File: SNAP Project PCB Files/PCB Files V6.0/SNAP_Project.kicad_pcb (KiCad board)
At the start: 4 copper layers, 66.7 x 47.2 mm, 107 parts, among them IC1 ADP121-AUJZ30R7, IC2 STM32WB35CCU7A, J1 USB_C_Receptacle_USB2.0, J3 Serial Wire Debug, J4 OLED Screen Conn, Q1 2N7000, Q2 2N7000, Q3 2N7000, Q4 SFH 310, Q5 2N7002KDW_R1_00001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

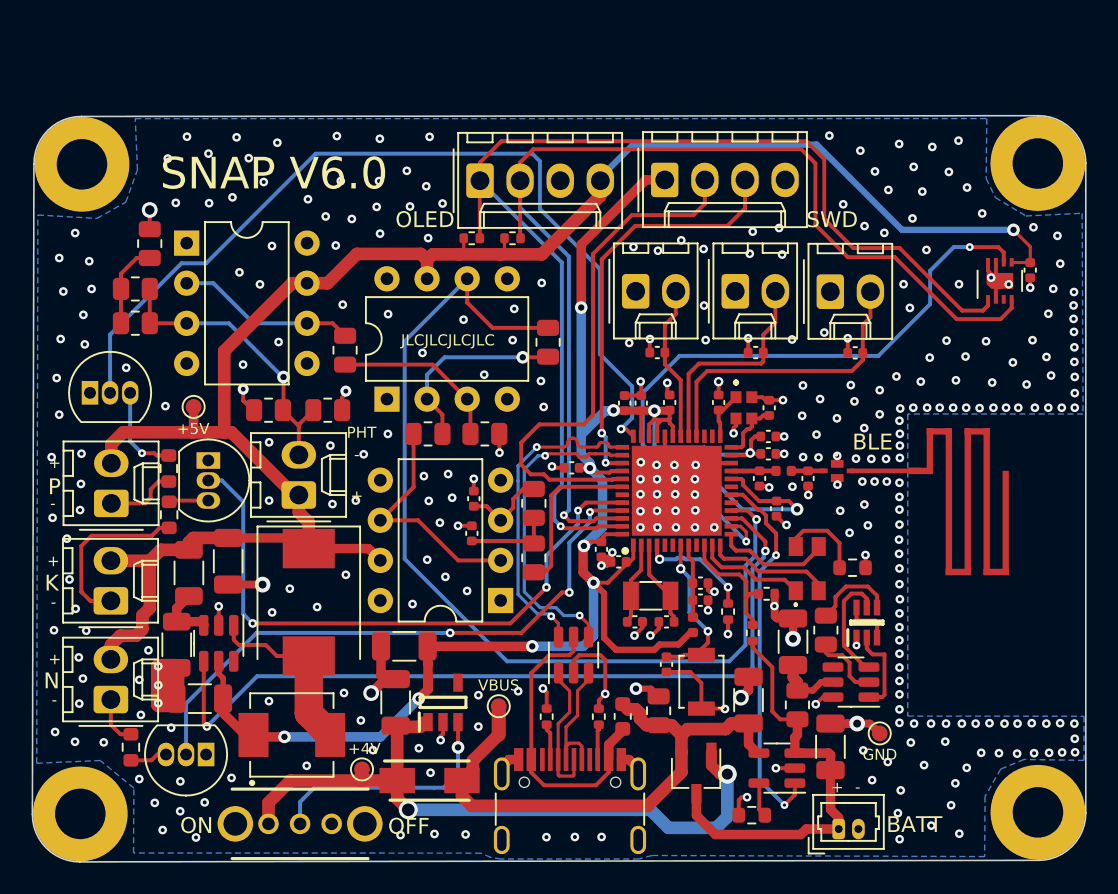
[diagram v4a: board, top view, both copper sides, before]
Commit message: OLED Screen Fix & Board corrections
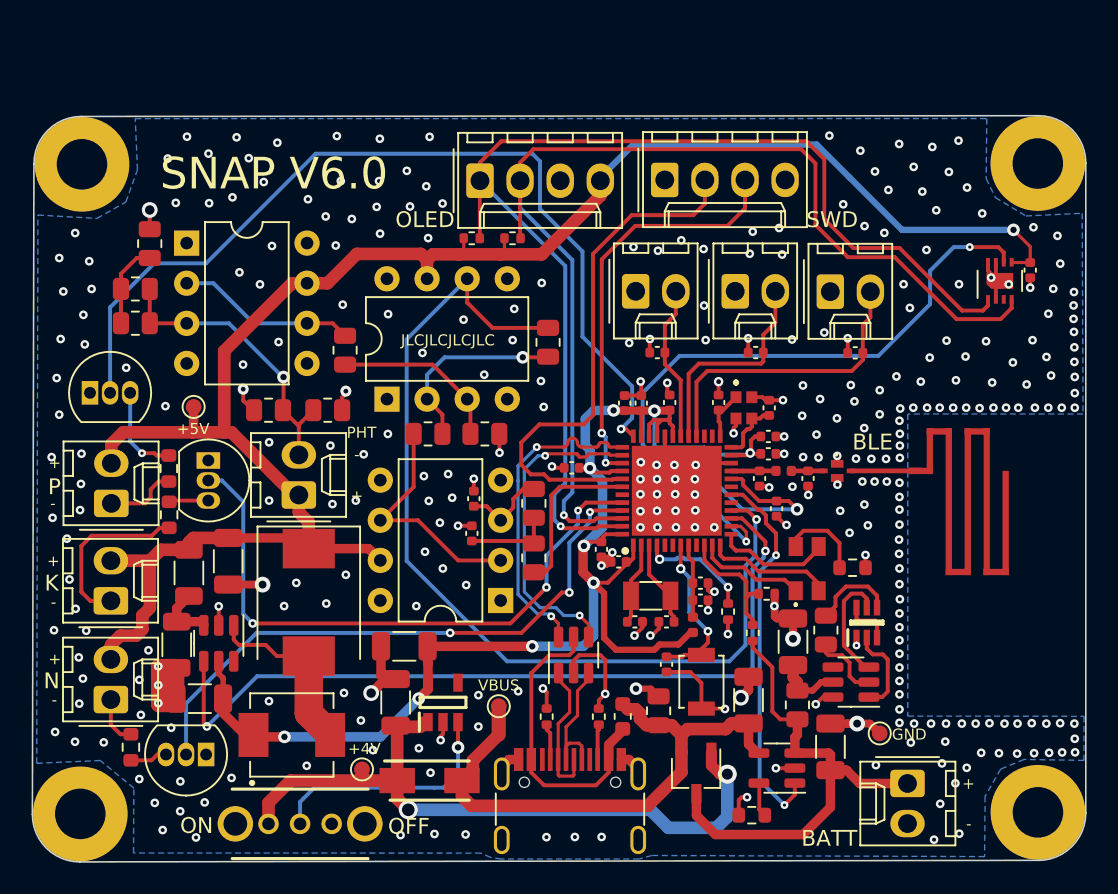
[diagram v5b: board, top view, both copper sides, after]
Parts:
- BT1: footprint Connector_Molex:Molex_PicoBlade_53047-0210_1x02_P1.25mm_Vertical -> Connector_Molex:Molex_KK-254_AE-6410-02A_1x02_P2.54mm_Vertical
- moved G*** 5.89 mm to (115.8, 111.6)
- moved BT1 5.23 mm to (122.2, 117.1), turned to -90 degrees
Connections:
- J3 pad 1: +3V0 -> unconnected-(J3-Pad1)
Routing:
- net +3V0: track 122.9 -> 104.2 mm, vias 11 -> 10
- net +BATT: track 27.2 -> 30.9 mm
- net WP7_EN: track 56.5 -> 57.5 mm
- net GND: vias 342 -> 337
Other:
- board text removed: "+3V0"

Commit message: New changes 1.0
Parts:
- removed C19, C20: 6p, Capacitor_SMD:C_0402_1005Metric
- moved R14 20.6 mm to (131.4, 87.2), turned to 90 degrees
- moved D6 18.8 mm to (129.5, 90.6), turned to 180 degrees
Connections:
- C8 pad 1: +5V -> +3V0
- D2 pad 2: +5V -> +3V0
- D3 pad 2: +5V -> +3V0
- D4 pad 2: +5V -> +3V0
- IC2 pad 9: unconnected-(IC2-Pad9) -> Feedback_VREF
- J4 pad 4: +5V -> +3V0
- R15 pad 1: +5V -> +3V0
- R16 pad 1: +5V -> +3V0
- R23 pad 1: Net-(R23-Pad1) -> Feedback_VREF
- U4 pad 5: +5V -> +3V0
- U5 pad 2: Net-(R23-Pad1) -> Feedback_VREF
- U5 pad 6: Net-(R23-Pad1) -> Feedback_VREF
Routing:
- net +3V0: track 104.2 -> 196.0 mm, vias 10 -> 12
- net +5V: track 117.7 -> 46.9 mm, vias 1 -> 0
- net Feedback_VREF: track 0.00 -> 37.4 mm, vias 0 -> 1
- net RGB_GREEN: track 7.31 -> 33.2 mm, vias 0 -> 2
- net RGB_RED: track 6.96 -> 29.8 mm, vias 0 -> 2
- net RGB_BLUE: track 8.05 -> 28.3 mm, vias 0 -> 2
- net Net-(R23-Pad1): track 15.0 -> 0.00 mm
- net Net-(D6-Pad2): track 5.37 -> 2.02 mm
- net BOOT0: track 7.14 -> 9.68 mm
- net GND: track 94.3 -> 92.3 mm, vias 337 -> 301
- net HSE_OUT: track 4.01 -> 2.74 mm
- net NRST: track 10.1 -> 10.7 mm
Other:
- board text added: "SNAP V6.1"
- board text removed: "SNAP V6.0"

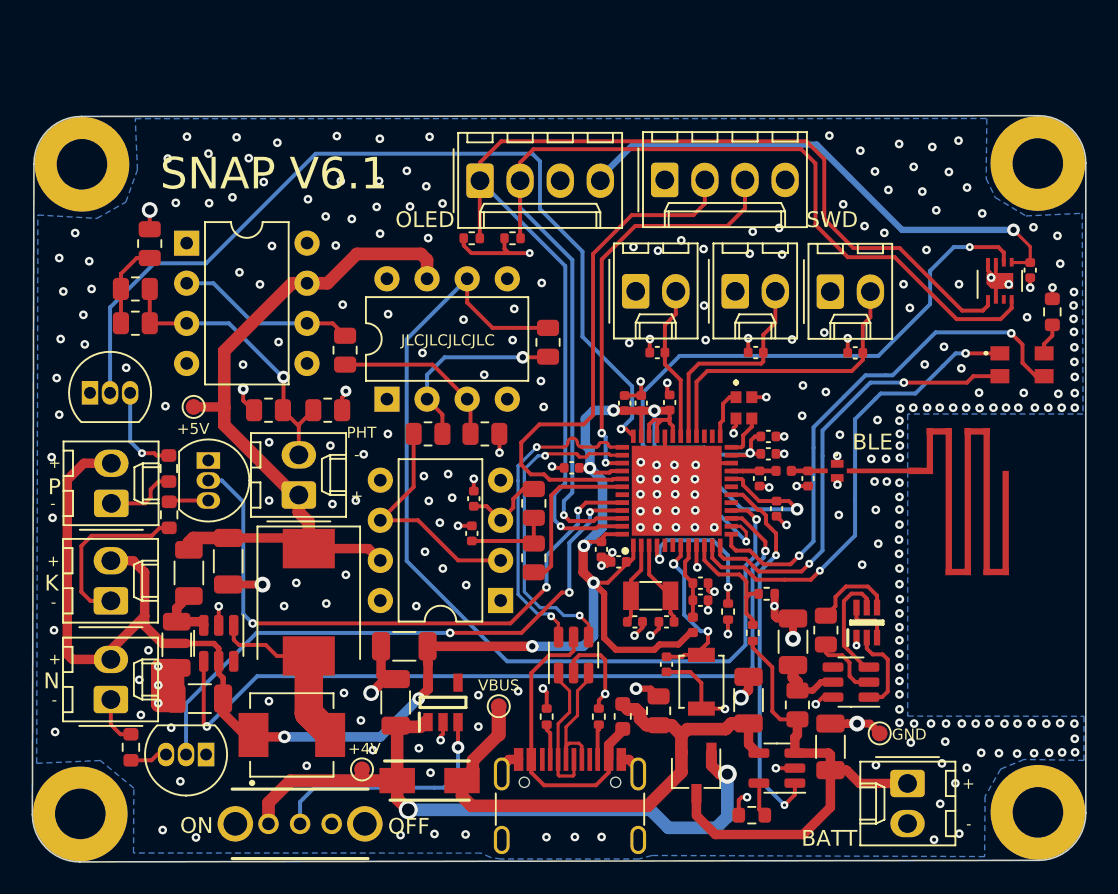
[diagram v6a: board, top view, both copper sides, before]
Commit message: Updated Connectors, LEDs, filter and STM I/O
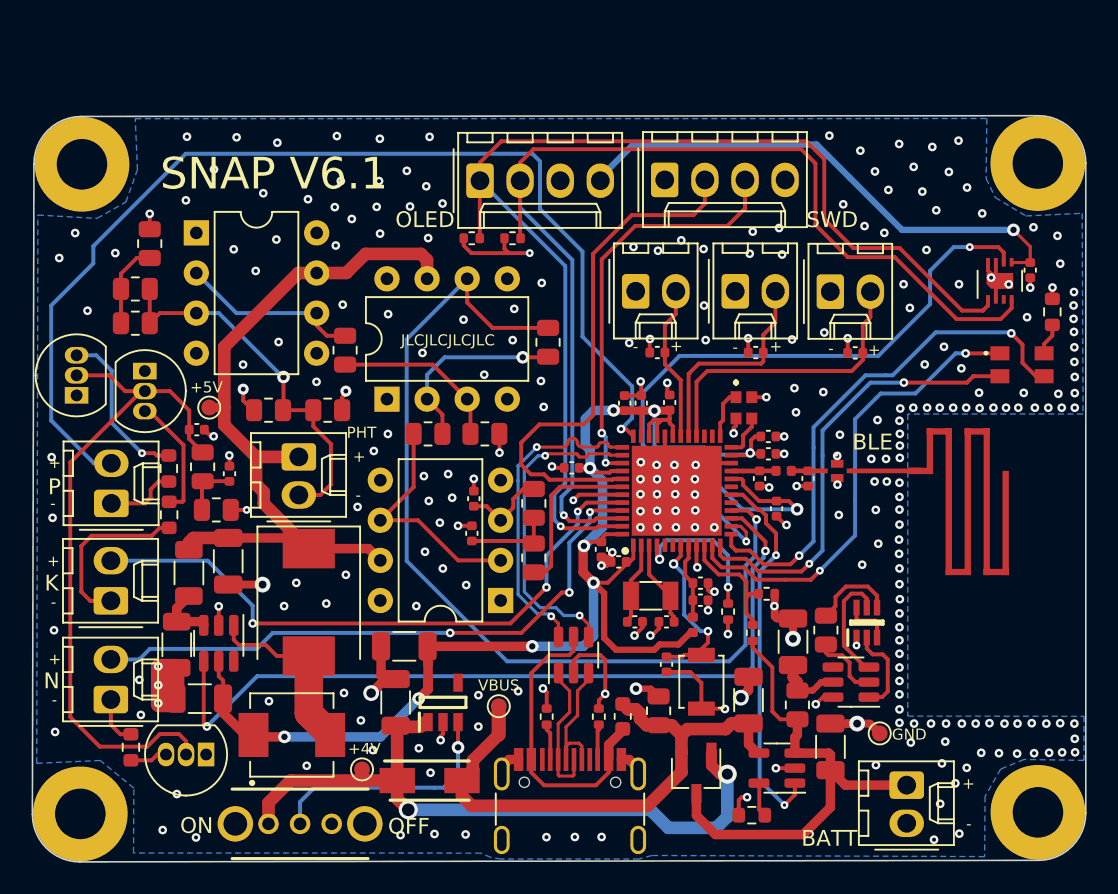
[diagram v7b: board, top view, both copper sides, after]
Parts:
- added C19: 0u1, Capacitor_SMD:C_0402_1005Metric, F.Cu at (79.3, 97.5)
- added C20: 10u, Capacitor_SMD:C_0402_1005Metric, F.Cu at (77.2, 94.7)
- added R29: 1k, Resistor_SMD:R_0805_2012Metric, F.Cu at (78.5, 99.8)
- added R30: 10k, Resistor_SMD:R_0805_2012Metric, F.Cu at (77.6, 97.0)
- R3: value 170 -> 250
- R4: value 120 -> 30
- R5: value 130 -> 40
- moved Q2 6.94 mm to (73.9, 91.0)
- moved BT1 2.52 mm to (122.2, 119.6), turned to 90 degrees
- moved TP2 0.99 mm to (78.0, 93.3)
- moved U6 0.89 mm to (77.2, 82.2)
- moved Q1 0.87 mm to (69.6, 92.5), turned to 90 degrees
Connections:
- D2 pad 2: +3V0 -> WP7_EN
- D3 pad 2: +3V0 -> 4273_EN
- D4 pad 2: +3V0 -> 4261_EN
- IC2 pad 43: unconnected-(IC2-Pad43) -> PWM_LEDS
- Q1 pad 2: WP7_EN -> FILT_PWM
- Q2 pad 2: 4273_EN -> FILT_PWM
- Q3 pad 2: 4261_EN -> FILT_PWM
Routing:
- net FILT_PWM: track 0.00 -> 43.3 mm
- net +3V0: track 196.0 -> 163.3 mm
- net PWM_LEDS: track 0.00 -> 27.6 mm, vias 0 -> 2
- net WP7_EN: track 57.5 -> 68.6 mm
- net Net-(Q4-Pad2): track 18.8 -> 24.1 mm
- net Net-(Q2-Pad3): track 2.51 -> 7.80 mm
- net Net-(Q1-Pad3): track 5.89 -> 10.4 mm
- net Net-(C19-Pad1): track 0.00 -> 3.89 mm
- net +5V: track 46.9 -> 48.6 mm
- net GND: track 92.3 -> 93.6 mm, vias 301 -> 286
- net 4273_EN: track 39.0 -> 39.5 mm

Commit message: Final Commit V 6.1
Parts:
- R23: value 3k3 -> 2k2
- R24: value 1k5 -> 4k7
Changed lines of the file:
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@@
       (drillshape 0)
       (scaleselection 1)
-      (outputdirectory "SNAP Gerbers/")
+      (outputdirectory "SNAP_6.1_Gerbers/")
     )
   )
@@
     (fp_line (start 1 0.625) (end -1 0.625) (layer "F.Fab") (width 0.1))
     (fp_line (start -1 0.625) (end -1 -0.625) (layer "F.Fab") (width 0.1))
-    (pad "1" smd roundrect (at -0.9125 0 180) (size 1.025 1.4) (layers "F.Cu" "F.Paste" "F.Mask") (roundrect_rratio 0.243902)
+    (pad "1" smd roundrect (at -0.9125 0 180) (size 1.025 1.4) (layers "F.Cu" "F.Paste" "F.Mask") (roundrect_rratio 0.243902439)
       (net 53 "Net-(Q4-Pad2)") (pintype "passive"))
-    (pad "2" smd roundrect (at 0.9125 0 180) (size 1.025 1.4) (layers "F.Cu" "F.Paste" "F.Mask") (roundrect_rratio 0.243902)
+    (pad "2" smd roundrect (at 0.9125 0 180) (size 1.025 1.4) (layers "F.Cu" "F.Paste" "F.Mask") (roundrect_rratio 0.243902439)
       (net 89 "Net-(R18-Pad2)") (pintype "passive"))
     (model "${KICAD6_3DMODEL_DIR}/Resistor_SMD.3dshapes/R_0805_2012Metric.wrl"
@@
     (fp_line (start 1 -0.625) (end 1 0.625) (layer "F.Fab") (width 0.1))
     (fp_line (start 1 0.625) (end -1 0.625) (layer "F.Fab") (width 0.1))
-    (pad "1" smd roundrect (at -0.9125 0 180) (size 1.025 1.4) (layers "F.Cu" "F.Paste" "F.Mask") (roundrect_rratio 0.243902)
+    (pad "1" smd roundrect (at -0.9125 0 180) (size 1.025 1.4) (layers "F.Cu" "F.Paste" "F.Mask") (roundrect_rratio 0.243902439)
       (net 53 "Net-(Q4-Pad2)") (pintype "passive"))
-    (pad "2" smd roundrect (at 0.9125 0 180) (size 1.025 1.4) (layers "F.Cu" "F.Paste" "F.Mask") (roundrect_rratio 0.243902)
+    (pad "2" smd roundrect (at 0.9125 0 180) (size 1.025 1.4) (layers "F.Cu" "F.Paste" "F.Mask") (roundrect_rratio 0.243902439)
       (net 89 "Net-(R18-Pad2)") (pintype "passive"))
     (model "${KICAD6_3DMODEL_DIR}/Resistor_SMD.3dshapes/R_0805_2012Metric.wrl"
@@
     (fp_line (start -1.27 2.88) (end 3.81 2.88) (layer "F.Fab") (width 0.1))
     (fp_line (start 3.81 -2.92) (end -1.27 -2.92) (layer "F.Fab") (width 0.1))
-    (pad "1" thru_hole roundrect (at 2.413 0 90) (size 1.74 2.19) (drill 1.19) (layers *.Cu *.Mask) (roundrect_rratio 0.143678)
+    (pad "1" thru_hole roundrect (at 2.413 0 90) (size 1.74 2.19) (drill 1.19) (layers *.Cu *.Mask) (roundrect_rratio 0.1436781609)
       (net 48 "+BATT") (pinfunction "+") (pintype "passive"))
     (pad "2" thru_hole oval (at 0 0 90) (size 1.74 2.19) (drill 1.19) (layers *.Cu *.Mask)
@@
     (fp_line (start -1 -0.625) (end 1 -0.625) (layer "F.Fab") (width 0.1))
     (fp_line (start 1 0.625) (end -1 0.625) (layer "F.Fab") (width 0.1))
-    (pad "1" smd roundrect (at -0.9125 0 90) (size 1.025 1.4) (layers "F.Cu" "F.Paste" "F.Mask") (roundrect_rratio 0.243902)
+    (pad "1" smd roundrect (at -0.9125 0 90) (size 1.025 1.4) (layers "F.Cu" "F.Paste" "F.Mask") (roundrect_rratio 0.243902439)
       (net 89 "Net-(R18-Pad2)") (pintype "passive"))
-    (pad "2" smd roundrect (at 0.9125 0 90) (size 1.025 1.4) (layers "F.Cu" "F.Paste" "F.Mask") (roundrect_rratio 0.243902)
+    (pad "2" smd roundrect (at 0.9125 0 90) (size 1.025 1.4) (layers "F.Cu" "F.Paste" "F.Mask") (roundrect_rratio 0.243902439)
       (net 2 "GND") (pintype "passive"))
     (model "${KICAD6_3DMODEL_DIR}/Resistor_SMD.3dshapes/R_0805_2012Metric.wrl"
@@
     (fp_line (start -1 0.625) (end -1 -0.625) (layer "F.Fab") (width 0.1))
     (fp_line (start -1 -0.625) (end 1 -0.625) (layer "F.Fab") (width 0.1))
-    (pad "1" smd roundrect locked (at -0.9125 0 90) (size 1.025 1.4) (layers "F.Cu" "F.Paste" "F.Mask") (roundrect_rratio 0.243902)
+    (pad "1" smd roundrect locked (at -0.9125 0 90) (size 1.025 1.4) (layers "F.Cu" "F.Paste" "F.Mask") (roundrect_rratio 0.243902439)
       (net 18 "Net-(C19-Pad1)") (pintype "passive"))
-    (pad "2" smd roundrect locked (at 0.9125 0 90) (size 1.025 1.4) (layers "F.Cu" "F.Paste" "F.Mask") (roundrect_rratio 0.243902)
+    (pad "2" smd roundrect locked (at 0.9125 0 90) (size 1.025 1.4) (layers "F.Cu" "F.Paste" "F.Mask") (roundrect_rratio 0.243902439)
       (net 68 "FILT_PWM") (pintype "passive"))
     (model "${KICAD6_3DMODEL_DIR}/Resistor_SMD.3dshapes/R_0805_2012Metric.wrl"
@@
       (effects (font (size 1 1) (thickness 0.15)))
     )
-    (fp_text value "3k3" (at 0 1.65) (layer "F.Fab") hide
+    (fp_text value "2k2" (at 0 1.65) (layer "F.Fab") hide
       (effects (font (size 1 1) (thickness 0.15)))
     )
@@
       (effects (font (size 1 1) (thickness 0.15)))
     )
-    (fp_text value "1k5" (at 0 1.65 90) (layer "F.Fab") hide
+    (fp_text value "4k7" (at 0 1.65 90) (layer "F.Fab") hide
       (effects (font (size 1 1) (thickness 0.15)))
     )
@@
     (fp_line (start 1 -0.625) (end 1 0.625) (layer "F.Fab") (width 0.1))
     (fp_line (start 1 0.625) (end -1 0.625) (layer "F.Fab") (width 0.1))
-    (pad "1" smd roundrect locked (at -0.9125 0 180) (size 1.025 1.4) (layers "F.Cu" "F.Paste" "F.Mask") (roundrect_rratio 0.243902)
+    (pad "1" smd roundrect locked (at -0.9125 0 180) (size 1.025 1.4) (layers "F.Cu" "F.Paste" "F.Mask") (roundrect_rratio 0.243902439)
       (net 92 "PWM_LEDS") (pintype "passive"))
-    (pad "2" smd roundrect locked (at 0.9125 0 180) (size 1.025 1.4) (layers "F.Cu" "F.Paste" "F.Mask") (roundrect_rratio 0.243902)
+    (pad "2" smd roundrect locked (at 0.9125 0 180) (size 1.025 1.4) (layers "F.Cu" "F.Paste" "F.Mask") (roundrect_rratio 0.243902439)
       (net 18 "Net-(C19-Pad1)") (pintype "passive"))
     (model "${KICAD6_3DMODEL_DIR}/Resistor_SMD.3dshapes/R_0805_2012Metric.wrl"
@@
       (effects (font (size 1 1) (thickness 0.15)))
     )
-    (fp_line (start 2.29 1.46) (end 2.54 1.99) (layer "F.SilkS") (width 0.12))
+    (fp_line (start 1.74 -2.43) (end 3.34 -2.43) (layer "F.SilkS") (width 0.12))
     (fp_line (start -1.67 -2) (end -1.67 2) (layer "F.SilkS") (width 0.12))
-    (fp_line (start -1.38 -3.03) (end -1.38 2.99) (layer "F.SilkS") (width 0.12))
     (fp_line (start -0.8 -3.03) (end -0.8 -2.43) (layer "F.SilkS") (width 0.12))
+    (fp_line (start -1.38 -3.03) (end -1.38 2.99) (layer "F.SilkS") (width 0.12))
+    (fp_line (start 2.29 2.99) (end 2.29 1.99) (layer "F.SilkS") (width 0.12))
+    (fp_line (start 2.29 1.46) (end 2.54 1.99) (layer "F.SilkS") (width 0.12))
     (fp_line (start 3.92 2.99) (end 3.92 -3.03) (layer "F.SilkS") (width 0.12))
-    (fp_line (start 1.74 -2.43) (end 3.34 -2.43) (layer "F.SilkS") (width 0.12))
+    (fp_line (start 3.34 -2.43) (end 3.34 -3.03) (layer "F.SilkS") (width 0.12))
     (fp_line (start 2.54 1.99) (end 2.54 2.99) (layer "F.SilkS") (width 0.12))
     (fp_line (start 0.25 1.46) (end 2.29 1.46) (layer "F.SilkS") (width 0.12))
-    (fp_line (start 1.74 -3.03) (end 1.74 -2.43) (layer "F.SilkS") (width 0.12))
-    (fp_line (start -0.8 -2.43) (end 0.8 -2.43) (layer "F.SilkS") (width 0.12))
-    (fp_line (start 3.34 -2.43) (end 3.34 -3.03) (layer "F.SilkS") (width 0.12))
-    (fp_line (start -1.38 2.99) (end 3.92 2.99) (layer "F.SilkS") (width 0.12))
+    (fp_line (start 0.25 2.99) (end 0.25 1.99) (layer "F.SilkS") (width 0.12))
     (fp_line (start 0.8 -2.43) (end 0.8 -3.03) (layer "F.SilkS") (width 0.12))
+    (fp_line (start -1.38 2.99) (end 3.92 2.99) (layer "F.SilkS") (width 0.12))
     (fp_line (start 0 2.99) (end 0 1.99) (layer "F.SilkS") (width 0.12))
+    (fp_line (start -0.8 -2.43) (end 0.8 -2.43) (layer "F.SilkS") (width 0.12))
     (fp_line (start 0 1.99) (end 2.54 1.99) (layer "F.SilkS") (width 0.12))
     (fp_line (start 0 1.99) (end 0.25 1.46) (layer "F.SilkS") (width 0.12))
-    (fp_line (start 0.25 2.99) (end 0.25 1.99) (layer "F.SilkS") (width 0.12))
-    (fp_line (start 2.29 2.99) (end 2.29 1.99) (layer "F.SilkS") (width 0.12))
+    (fp_line (start 1.74 -3.03) (end 1.74 -2.43) (layer "F.SilkS") (width 0.12))
     (fp_line (start 3.92 -3.03) (end -1.38 -3.03) (layer "F.SilkS") (width 0.12))
+    (fp_line (start -1.77 -3.42) (end -1.77 3.38) (layer "F.CrtYd") (width 0.05))
     (fp_line (start 4.31 3.38) (end 4.31 -3.42) (layer "F.CrtYd") (width 0.05))
     (fp_line (start -1.77 3.38) (end 4.31 3.38) (layer "F.CrtYd") (width 0.05))
-    (fp_line (start -1.77 -3.42) (end -1.77 3.38) (layer "F.CrtYd") (width 0.05))
     (fp_line (start 4.31 -3.42) (end -1.77 -3.42) (layer "F.CrtYd") (width 0.05))
     (fp_line (start 3.81 2.88) (end 3.81 -2.92) (layer "F.Fab") (width 0.1))
@@
     (fp_line (start -1.27 -2.92) (end -1.27 2.88) (layer "F.Fab") (width 0.1))
     (fp_line (start -0.562893 0) (end -1.27 0.5) (layer "F.Fab") (width 0.1))
-    (pad "1" thru_hole roundrect (at 2.413 0 90) (size 1.74 2.19) (drill 1.19) (layers *.Cu *.Mask) (roundrect_rratio 0.143678)
+    (pad "1" thru_hole roundrect (at 2.413 0 90) (size 1.74 2.19) (drill 1.19) (layers *.Cu *.Mask) (roundrect_rratio 0.1436781609)
       (net 4 "+5V") (pinfunction "C") (pintype "passive"))
     (pad "2" thru_hole oval (at 0 0 90) (size 1.74 2.19) (drill 1.19) (layers *.Cu *.Mask)
